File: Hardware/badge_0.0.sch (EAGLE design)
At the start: 46 parts, among them CON1 PH_2, IC1 CP2102, SW1 MK12C02, SW2 MK12C02, U4 MCP73832T-2DCI/OT

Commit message: moved ESP to the opposite end w.r.t. LCD
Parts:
- removed J10: (no value), SparkFun-Connectors:M14
- removed J5: (no value), SparkFun-Connectors:M05PTH
- removed J8: (no value), SparkFun-Connectors:M10SILK_FEMALE_PTH
- J3: device SparkFun-Connectors:M12PTH -> SparkFun-Connectors:M16PTH
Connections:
- net ADC: no longer J8.7
- net CH_PD: no longer J8.6
- net CS0: now also J3.11; no longer J10.1, J3.12
- net GND: now also J3.15, J3.16; no longer J10.11, J10.12, J8.8
- net GPIO0: no longer J10.10
- net GPIO10: now also J3.5; no longer J10.5, J4.8
- net GPIO12/SPI_SO: now also J3.6; no longer J3.4, J8.5
- net GPIO13/SPI_SI: now also J3.7; no longer J3.5, J8.4
- net GPIO14/SPI_CLK/SCL: now also J3.8; no longer J3.6, J8.3
- net GPIO15/SPI_CS: now also J3.9; no longer J3.7, J8.2
- net GPIO16: now also J3.10; no longer J3.8, J8.1
- net GPIO2/SDA: now also U$2.P$2; no longer J10.9, U$3.P$2
- net GPIO4: now also U$4.P$2; no longer J10.8, U$2.P$2
- net GPIO5: now also U$3.P$2; no longer J10.7, U$4.P$2
- net GPIO9: now also J3.4; no longer J10.6, J4.7
- net MISO: now also J3.12; no longer J10.2, J3.11
- net MOSI: now also J3.13; no longer J10.3, J3.10
- net RX: no longer J10.13
- net SCLK: now also J3.14; no longer J10.4, J3.9
- net TX: no longer J10.14
- net VCC: now also J4.7, J4.8; no longer J8.10, J8.9

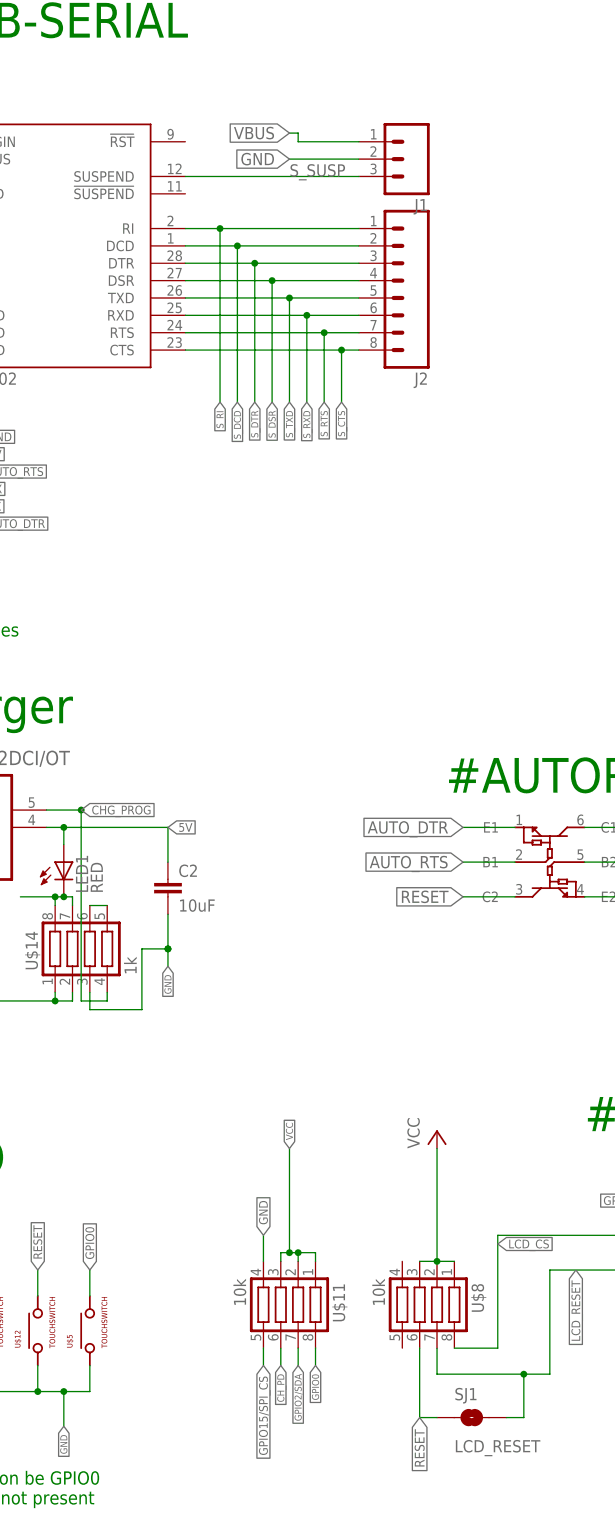
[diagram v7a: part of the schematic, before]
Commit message: Added !susp to serial headers. Rerouted many traces
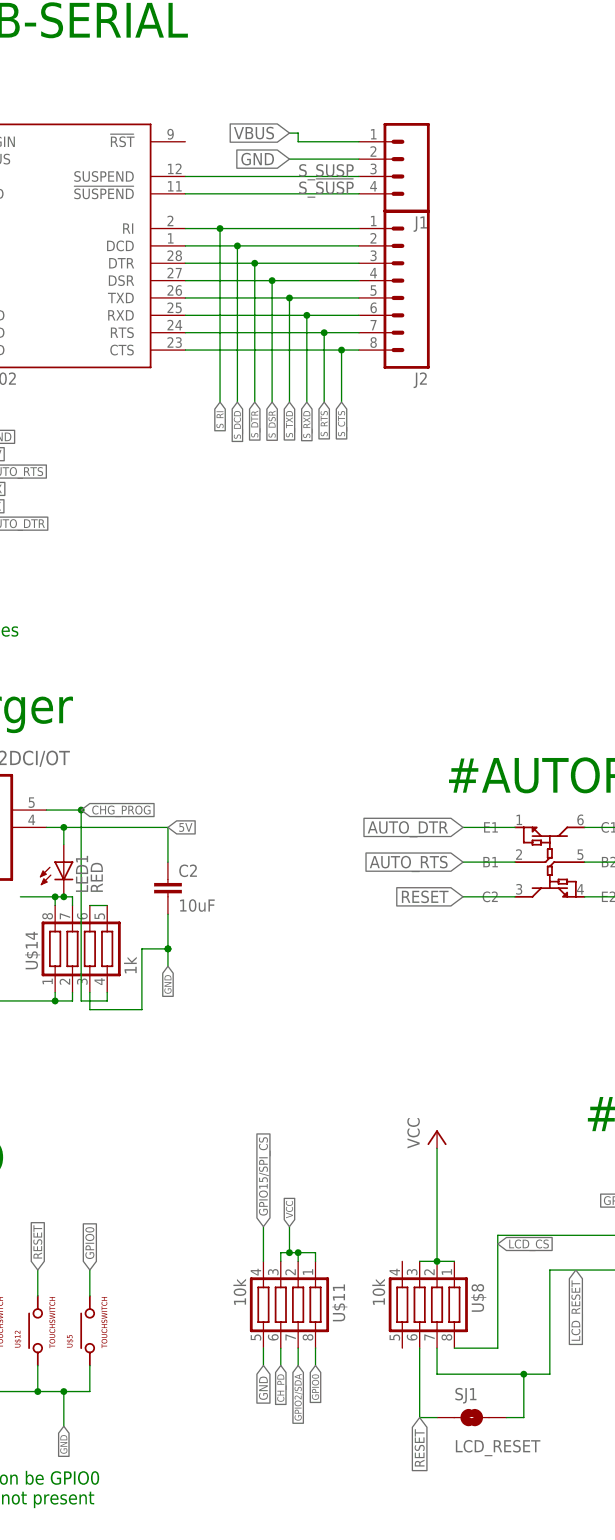
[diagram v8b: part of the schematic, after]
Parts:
- J1: device SparkFun-Connectors:M03PTH -> SparkFun-Connectors:M04PTH
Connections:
- new net S_!SUSP: IC1.!SUSPEND, J1.4
- net GND: now also U$11.5; no longer U$11.4
- net GPIO15/SPI_CS: now also U$11.4; no longer U$11.5
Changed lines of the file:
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@@
 <?xml version="1.0" encoding="utf-8"?>
 <!DOCTYPE eagle SYSTEM "eagle.dtd">
-<eagle version="7.5.0">
+<eagle version="7.1.0">
 <drawing>
 <settings>
@@
 <part name="IC1" library="silabs" deviceset="CP210*" device="" technology="2"/>
 <part name="J2" library="SparkFun-Connectors" deviceset="M08" device="SILK_FEMALE_PTH"/>
-<part name="J1" library="SparkFun-Connectors" deviceset="M03" device="PTH"/>
+<part name="J1" library="SparkFun-Connectors" deviceset="M04" device="PTH"/>
 <part name="C3" library="resistor" deviceset="C-EU" device="C0603K" value="10uF"/>
 <part name="LED3" library="led" deviceset="LED" device="SML0805"/>
@@
 <instance part="IC1" gate="G$1" x="81.28" y="213.36"/>
 <instance part="J2" gate="G$1" x="132.08" y="208.28" rot="R180"/>
-<instance part="J1" gate="J$1" x="134.62" y="226.06" rot="R180"/>
+<instance part="J1" gate="G$1" x="132.08" y="226.06" rot="R180"/>
 <instance part="C3" gate="G$1" x="48.26" y="213.36"/>
 <instance part="LED3" gate="G$1" x="295.91" y="71.12"/>
@@
 </segment>
 <segment>
-<label x="116.84" y="81.28" size="1.016" layer="95" rot="R90" xref="yes"/>
+<label x="116.84" y="69.85" size="1.016" layer="95" rot="R90" xref="yes"/>
 <pinref part="U$11" gate="G$1" pin="1"/>
 <wire x1="115.57" y1="66.04" x2="116.84" y2="66.04" width="0.1524" layer="91"/>
@@
 <wire x1="115.57" y1="66.04" x2="115.57" y2="64.77" width="0.1524" layer="91"/>
 <junction x="116.84" y="66.04"/>
-<wire x1="116.84" y1="66.04" x2="116.84" y2="81.28" width="0.1524" layer="91"/>
+<wire x1="116.84" y1="66.04" x2="116.84" y2="69.85" width="0.1524" layer="91"/>
 </segment>
 <segment>
@@
 </segment>
 <segment>
-<pinref part="J1" gate="J$1" pin="2"/>
+<pinref part="J1" gate="G$1" pin="2"/>
 <wire x1="127" y1="226.06" x2="116.84" y2="226.06" width="0.1524" layer="91"/>
 <label x="116.84" y="226.06" size="1.778" layer="95" rot="R180" xref="yes"/>
@@
 </segment>
 <segment>
-<pinref part="U$11" gate="G$1" pin="4"/>
-<wire x1="113.03" y1="64.77" x2="113.03" y2="68.58" width="0.1524" layer="91"/>
-<label x="113.03" y="68.58" size="1.27" layer="95" rot="R90" xref="yes"/>
-</segment>
-<segment>
 <pinref part="J3" gate="G$1" pin="16"/>
 <wire x1="213.36" y1="132.08" x2="209.55" y2="132.08" width="0.1524" layer="91"/>
@@
 <wire x1="213.36" y1="134.62" x2="209.55" y2="134.62" width="0.1524" layer="91"/>
 <label x="213.36" y="134.62" size="1.016" layer="95" xref="yes"/>
+</segment>
+<segment>
+<pinref part="U$11" gate="G$1" pin="5"/>
+<wire x1="113.03" y1="49.53" x2="113.03" y2="52.07" width="0.1524" layer="91"/>
+<label x="113.03" y="49.53" size="1.27" layer="95" ratio="6" rot="R270" xref="yes"/>
 </segment>
 </net>
@@
 </segment>
 <segment>
-<pinref part="U$11" gate="G$1" pin="5"/>
-<wire x1="113.03" y1="52.07" x2="113.03" y2="49.53" width="0.1524" layer="91"/>
-<label x="113.03" y="49.53" size="1.27" layer="95" rot="R270" xref="yes"/>
+<pinref part="U$11" gate="G$1" pin="4"/>
+<wire x1="113.03" y1="69.85" x2="113.03" y2="64.77" width="0.1524" layer="91"/>
+<label x="113.03" y="69.85" size="1.27" layer="95" ratio="6" rot="R90" xref="yes"/>
 </segment>
 <segment>
@@
 </segment>
 <segment>
-<pinref part="J1" gate="J$1" pin="1"/>
+<pinref part="J1" gate="G$1" pin="1"/>
 <wire x1="127" y1="228.6" x2="118.11" y2="228.6" width="0.1524" layer="91"/>
 <wire x1="118.11" y1="228.6" x2="118.11" y2="229.87" width="0.1524" layer="91"/>
@@
 <wire x1="63.5" y1="220.98" x2="48.26" y2="220.98" width="0.1524" layer="91"/>
 <wire x1="48.26" y1="220.98" x2="48.26" y2="215.9" width="0.1524" layer="91"/>
-</segment>
-</net>
-<net name="S_SUSP" class="0">
-<segment>
-<pinref part="IC1" gate="G$1" pin="SUSPEND"/>
-<pinref part="J1" gate="J$1" pin="3"/>
-<wire x1="101.6" y1="223.52" x2="127" y2="223.52" width="0.1524" layer="91"/>
-<label x="116.84" y="223.52" size="1.778" layer="95"/>
 </segment>
 </net>
@@
 </segment>
 </net>
+<net name="S_SUSP" class="0">
+<segment>
+<pinref part="J1" gate="G$1" pin="3"/>
+<wire x1="101.6" y1="223.52" x2="127" y2="223.52" width="0.1524" layer="91"/>
+<label x="118.11" y="223.52" size="1.778" layer="95"/>
+<pinref part="IC1" gate="G$1" pin="SUSPEND"/>
+</segment>
+</net>
+<net name="S_!SUSP" class="0">
+<segment>
+<pinref part="J1" gate="G$1" pin="4"/>
+<wire x1="101.6" y1="220.98" x2="127" y2="220.98" width="0.1524" layer="91"/>
+<label x="118.11" y="220.98" size="1.778" layer="95"/>
+<pinref part="IC1" gate="G$1" pin="!SUSPEND"/>
+</segment>
+</net>
